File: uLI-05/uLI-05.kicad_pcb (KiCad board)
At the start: 2 copper layers, 58 x 39.5 mm, 51 parts, among them J1 STL1550, J2 USB_B, J3 RJ25, J4 RJ25, J5 PROG, Q1 IRF7306, U1 LM78M05_TO252, U2 PC817, U3 PC817, U4 PIC18F14K50-EP, U5 ADM2483xRW, U6 USBLC6-2SC6, Y1 12MHz

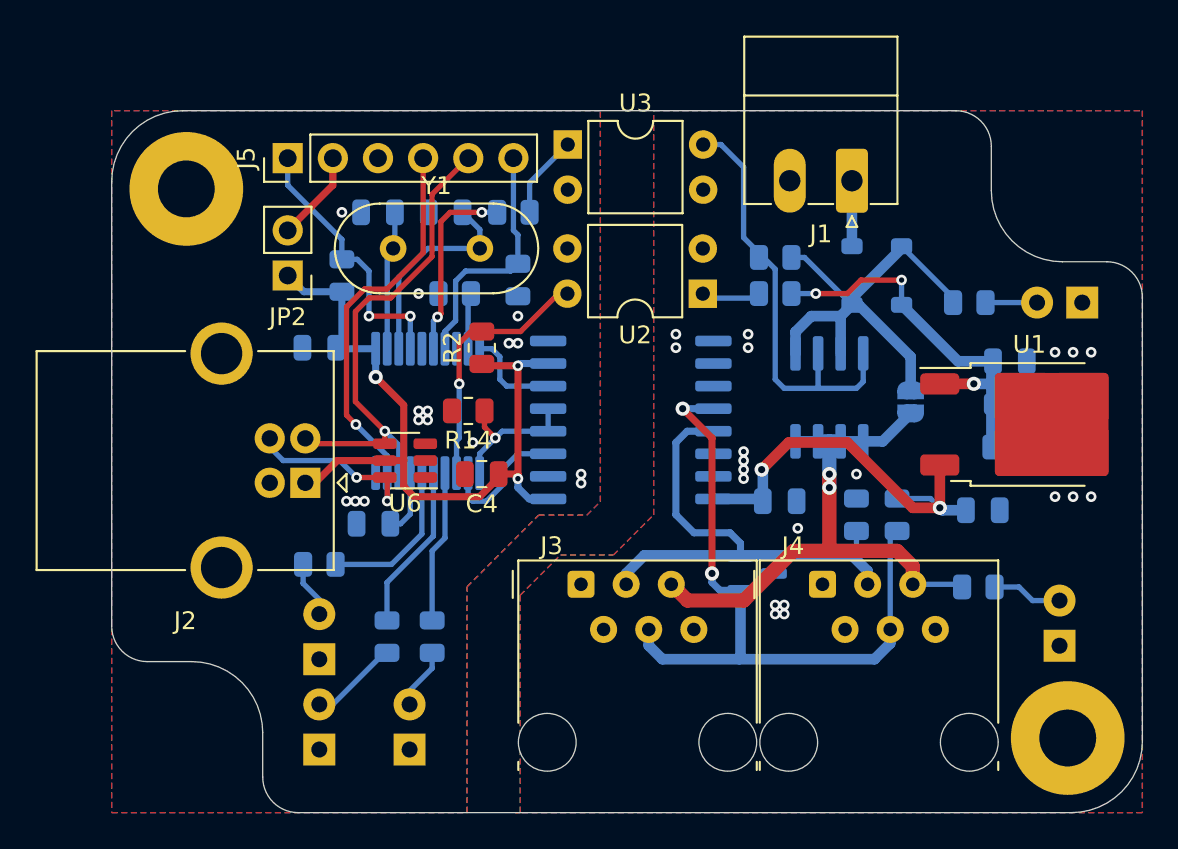
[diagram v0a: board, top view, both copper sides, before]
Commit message: Tweak silkscreen.
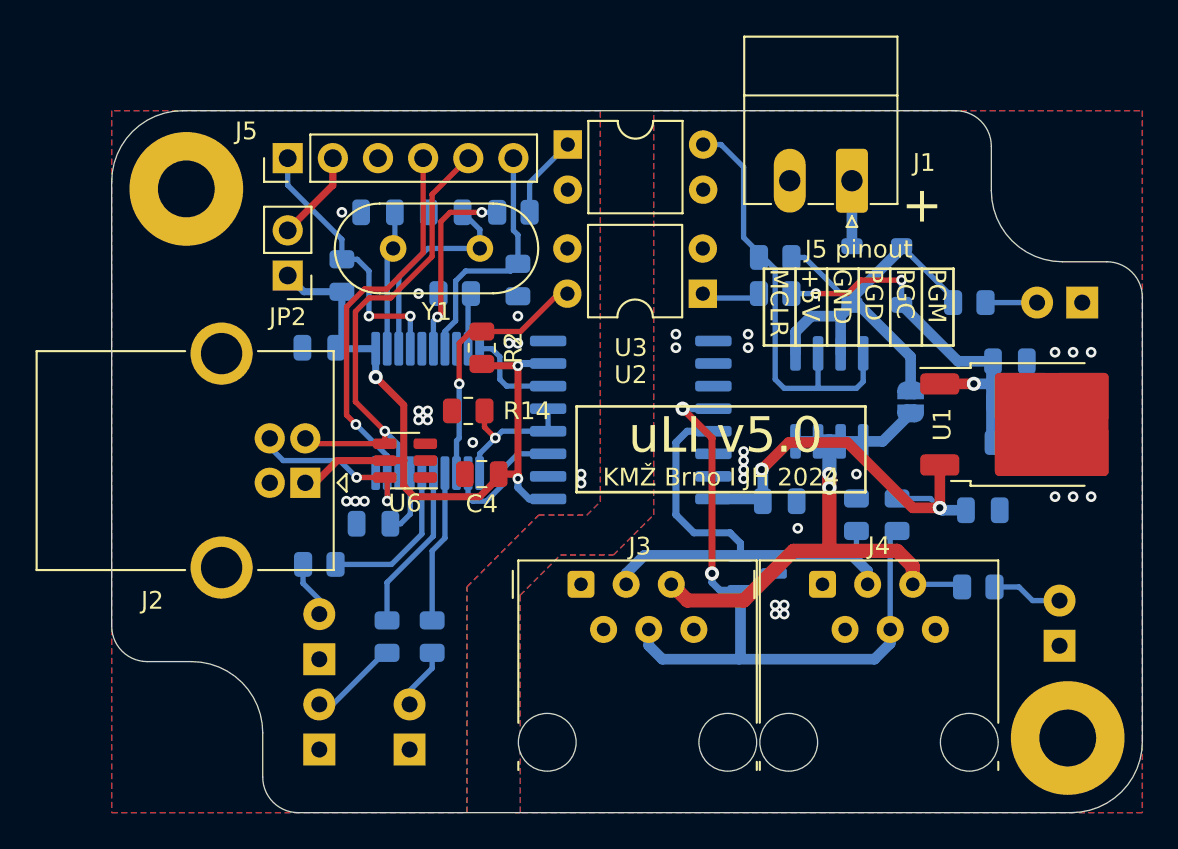
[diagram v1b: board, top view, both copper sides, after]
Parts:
- moved R13 0.28 mm to (176.9, 101.1)
- moved C10 0.25 mm to (180.5, 101.1)
- moved D3 0.18 mm to (177.7, 98.8)
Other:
- board text added: "+"
- board text added: "+5V"
- board text added: "GND"
- board text added: "J5 pinout"
- board text added: "KMŽ Brno I JH 2024"
- board text added: "MCLR"
- board text added: "PGC"
- board text added: "PGD"
- board text added: "PGM"
- board text added: "uLI v5.0"

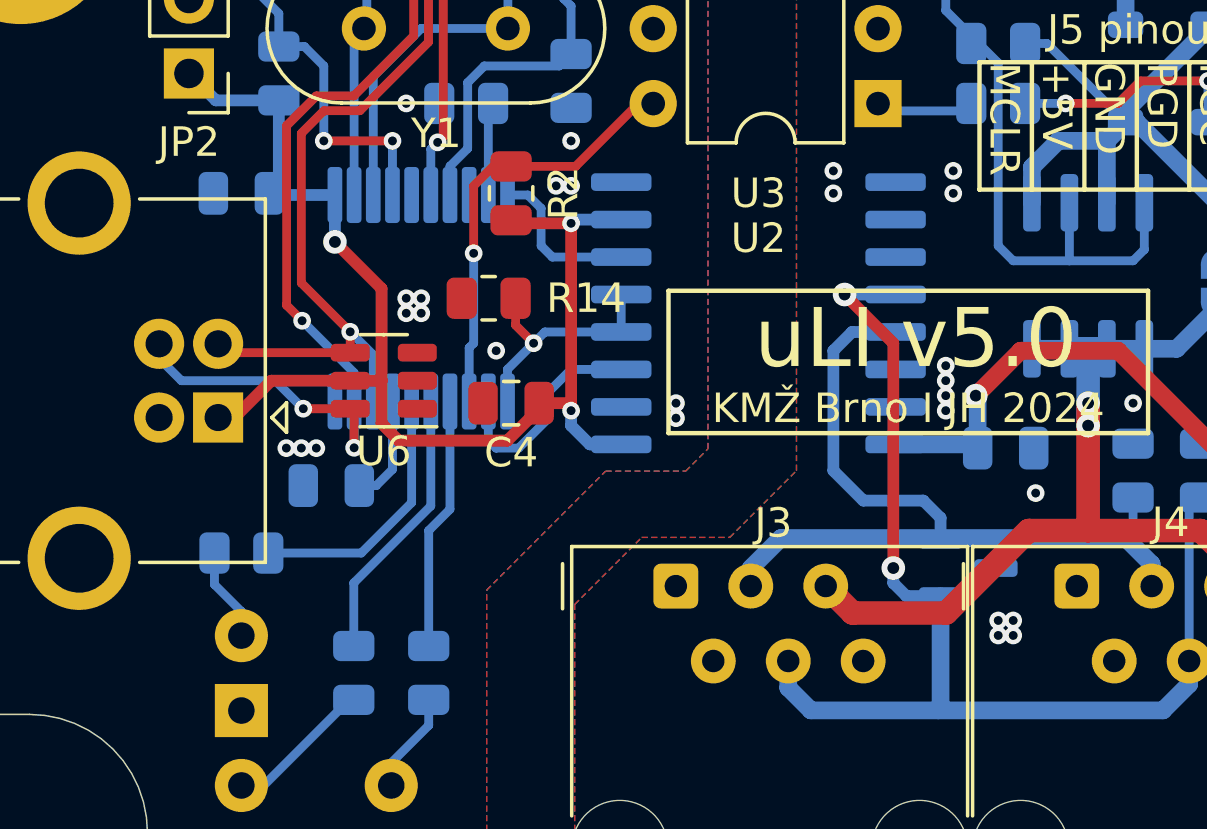
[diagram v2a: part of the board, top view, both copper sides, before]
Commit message: Fix issues reported by DRC.
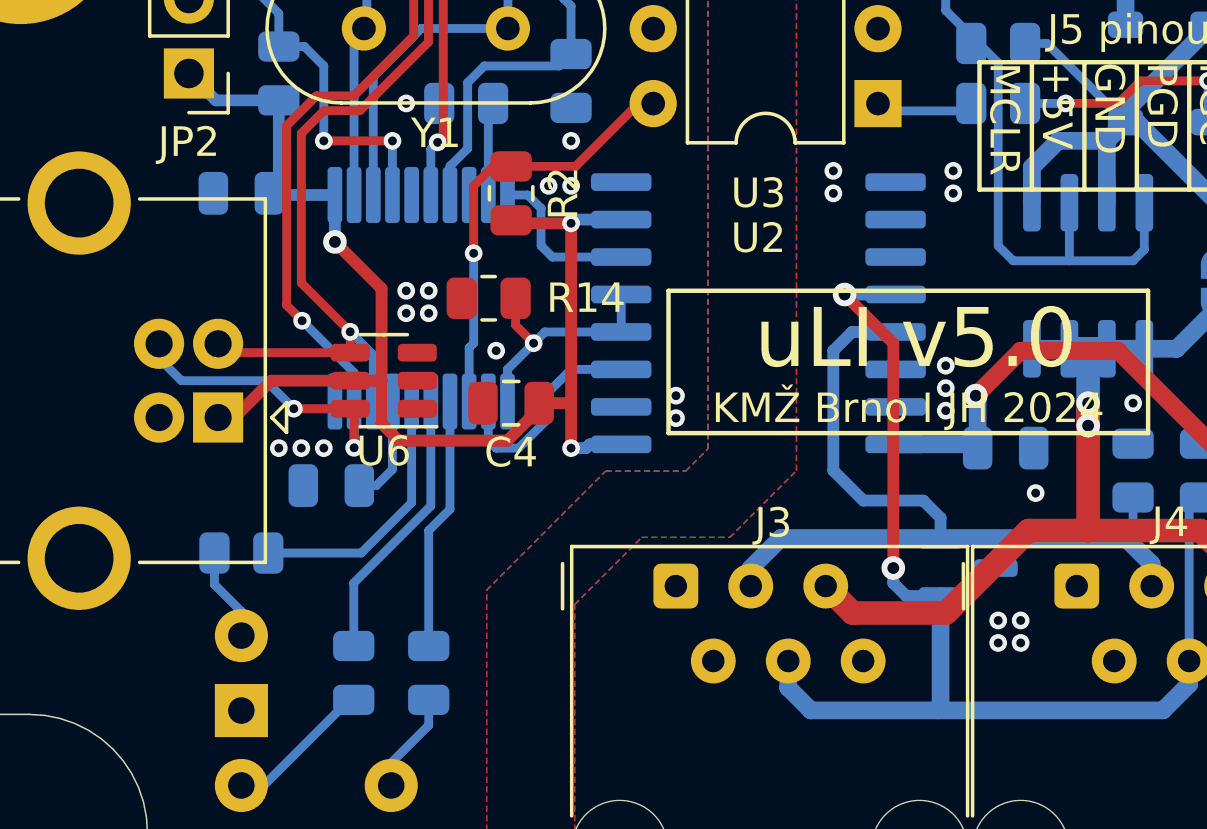
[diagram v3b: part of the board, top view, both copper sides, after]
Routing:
- net VCC: track 43.7 -> 44.2 mm
- net GNDA: vias 20 -> 19

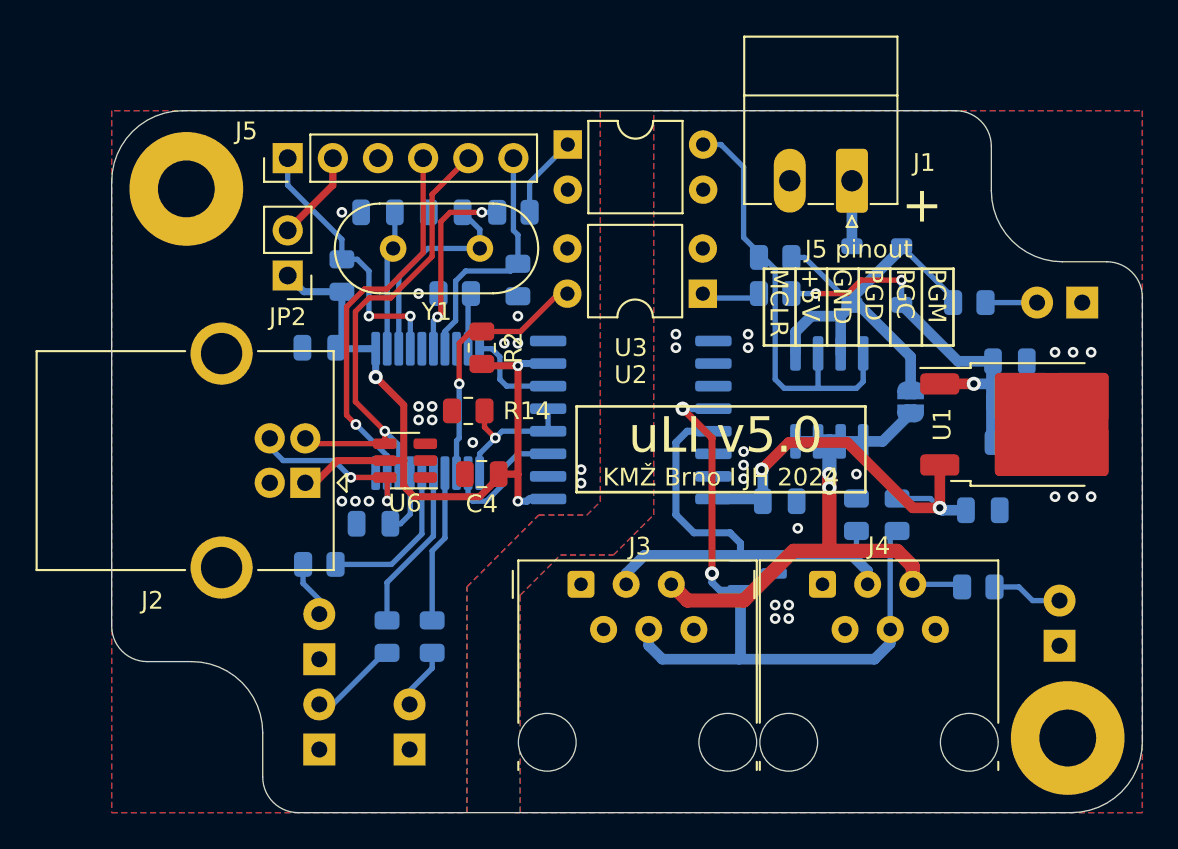
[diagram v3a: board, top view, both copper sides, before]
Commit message: Add fuses.
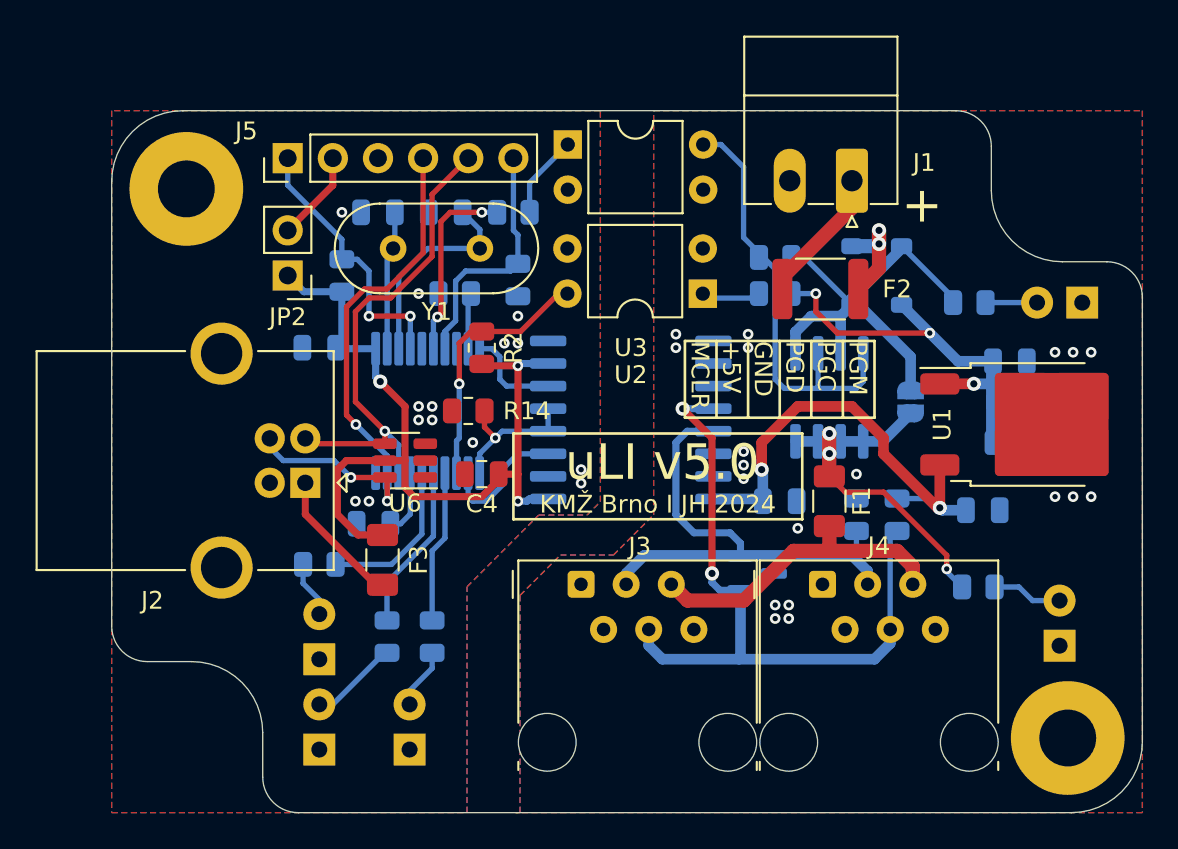
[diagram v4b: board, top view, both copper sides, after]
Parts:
- added F1: 200/400mA, Fuse:Fuse_1206_3216Metric, F.Cu at (166.8, 104.4)
- added F2: 750mA/1.5A, Fuse:Fuse_1812_4532Metric, F.Cu at (166.3, 92.5)
- added F3: 100/250mA, Fuse:Fuse_1206_3216Metric, F.Cu at (141.6, 107.7)
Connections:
- J1 pad 1: Net-(D2-A) -> Net-(J1-Pin_1)
- J2 pad 1: VCC -> Net-(J2-VBUS)
- J3 pad 5: /12VXN -> Net-(F1-Pad2)
- J4 pad 5: /12VXN -> Net-(F1-Pad2)
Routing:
- net Net-(F1-Pad2): track 0.00 -> 17.9 mm
- net /12VXN: track 33.4 -> 21.3 mm, vias 2 -> 3
- net Net-(J2-VBUS): track 0.00 -> 8.31 mm
- net Net-(J1-Pin_1): track 0.00 -> 7.72 mm
- net Net-(D1-K): track 22.1 -> 25.8 mm
- net VCC: track 44.2 -> 47.8 mm
- net +5VA: track 23.4 -> 26.5 mm
- net Net-(D2-A): track 3.68 -> 6.38 mm, vias 0 -> 2
- net GND: vias 15 -> 14
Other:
- board text removed: "J5 pinout"

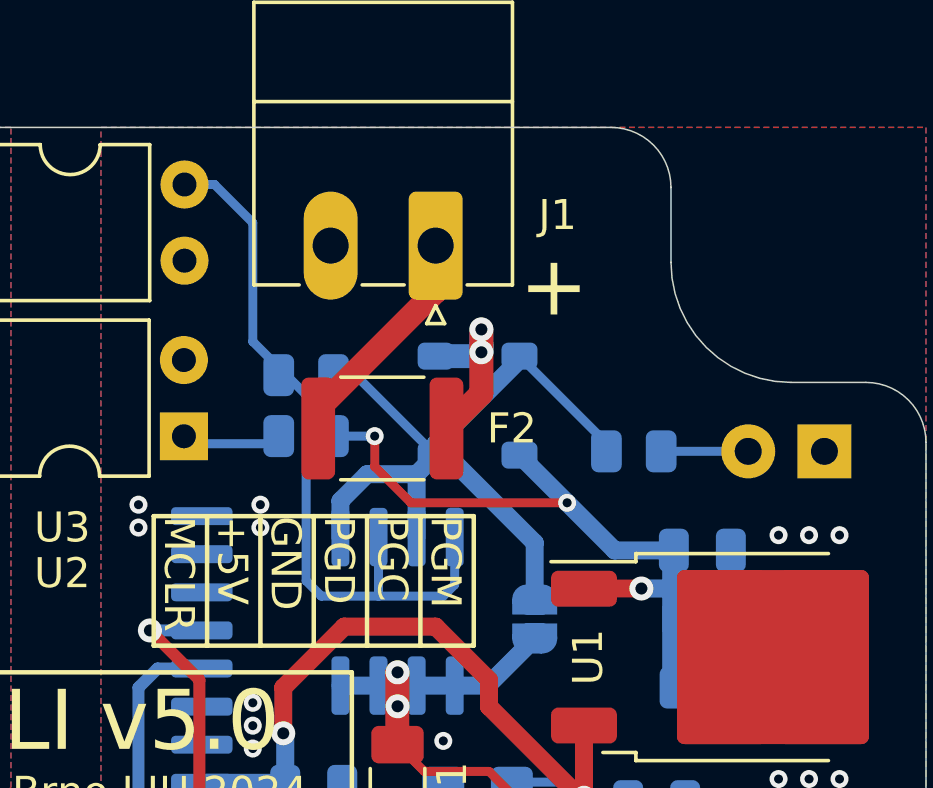
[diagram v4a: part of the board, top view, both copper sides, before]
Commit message: Use SS34 as D2.
SS34 supports larger maximum current.
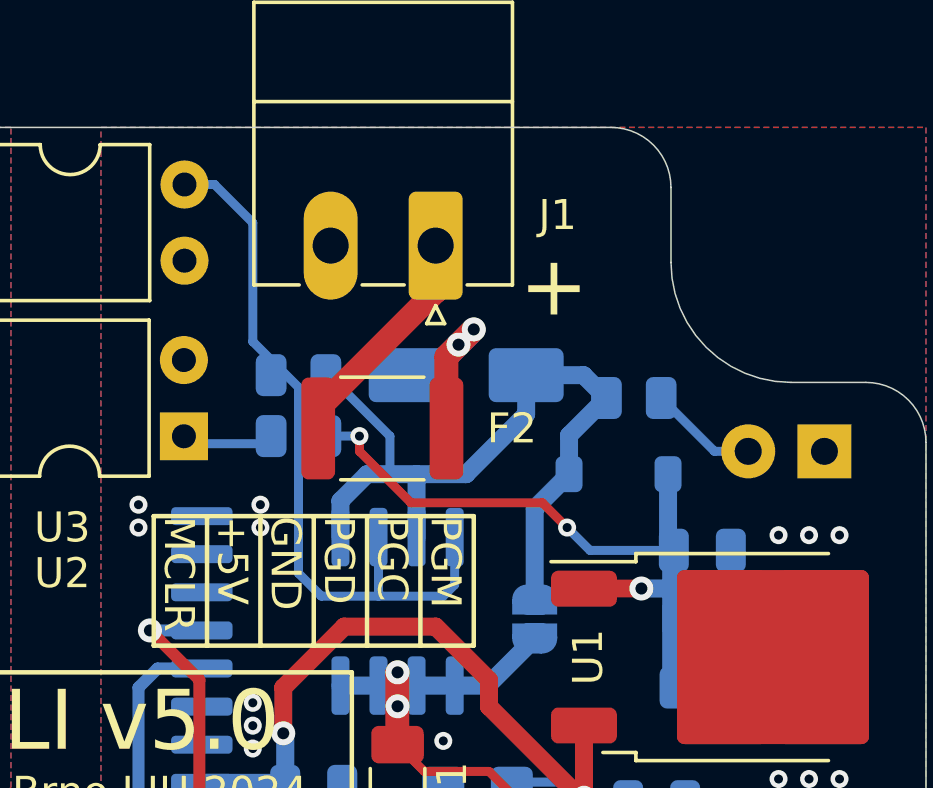
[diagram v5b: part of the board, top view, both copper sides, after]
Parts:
- D2: value 1N5819 -> SS34; footprint Diode_SMD:D_SOD-123 -> Diode_SMD:D_SMA
- moved D1 4.02 mm to (174.1, 94.0), turned to 180 degrees
- moved R8 1.78 mm to (174.6, 91.5)
- moved D2 1.44 mm to (169.0, 90.7), turned to 180 degrees
- moved R1 0.25 mm to (163.5, 92.7)
- moved R10 0.25 mm to (163.5, 90.7)
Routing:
- net Net-(D1-K): track 25.8 -> 23.6 mm
- net Net-(D4-A): track 2.90 -> 3.64 mm
